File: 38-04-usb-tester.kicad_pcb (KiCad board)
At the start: 2 copper layers, 101.7 x 101.7 mm, 33 parts, among them J1 USB3_A, J2 USB_B_Micro, J3 USB_C_Receptacle, J4 USB_B_Mini

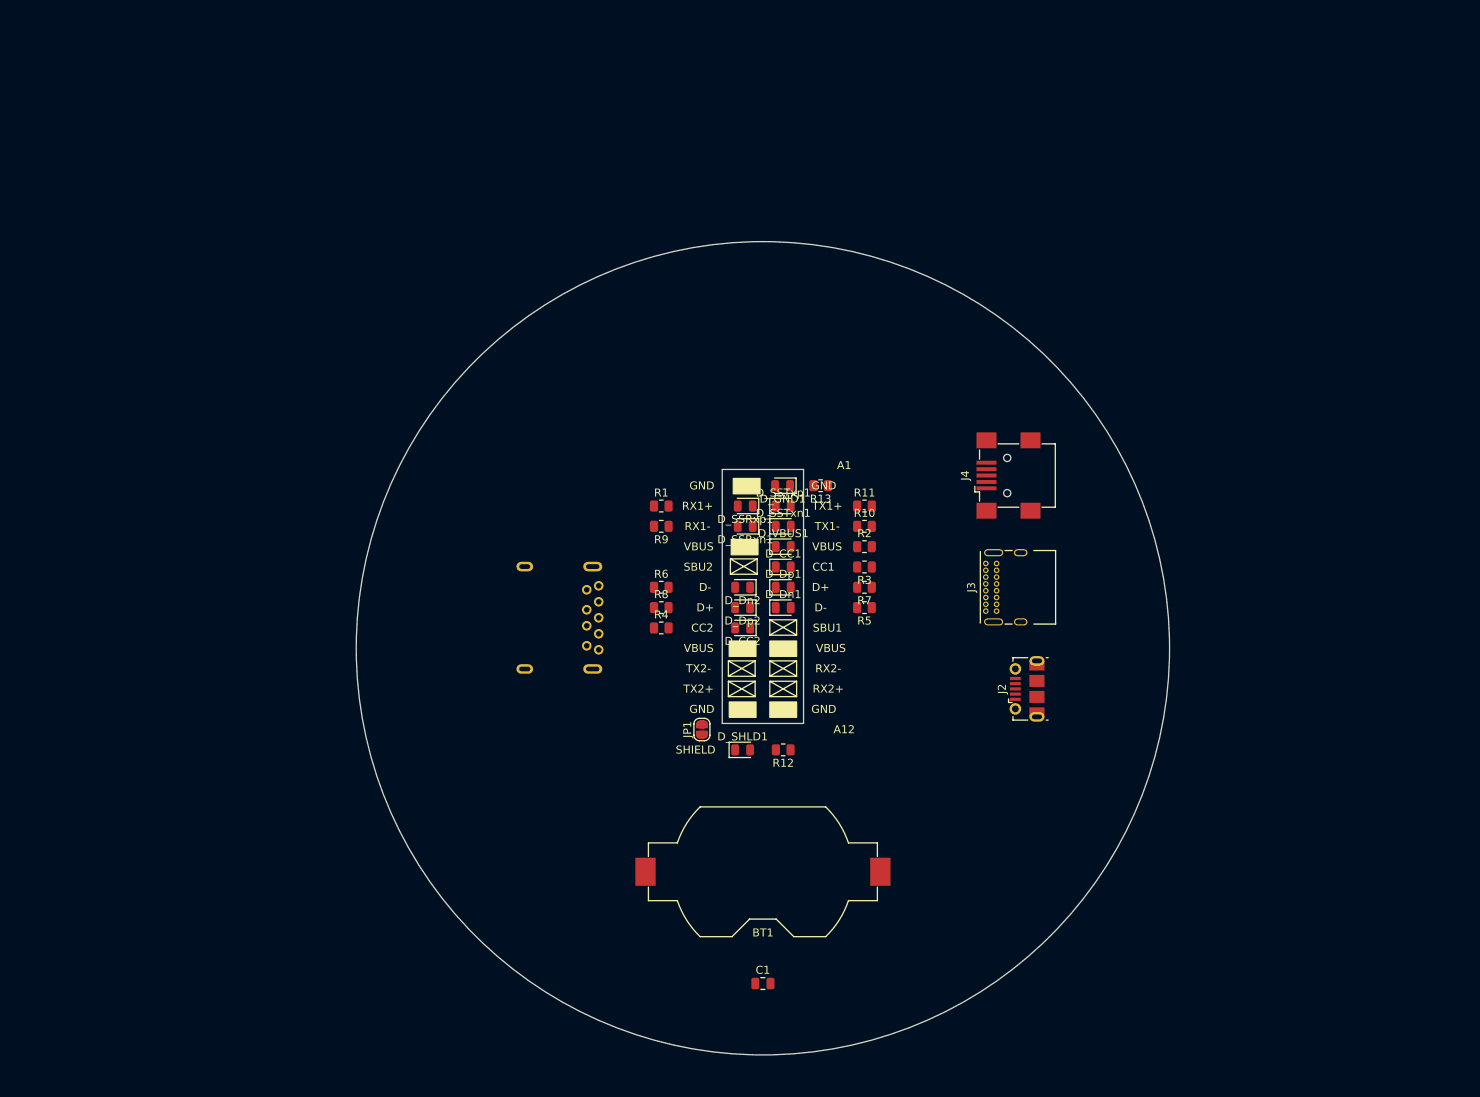
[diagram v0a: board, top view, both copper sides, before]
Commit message: added new footprints, schematic edits
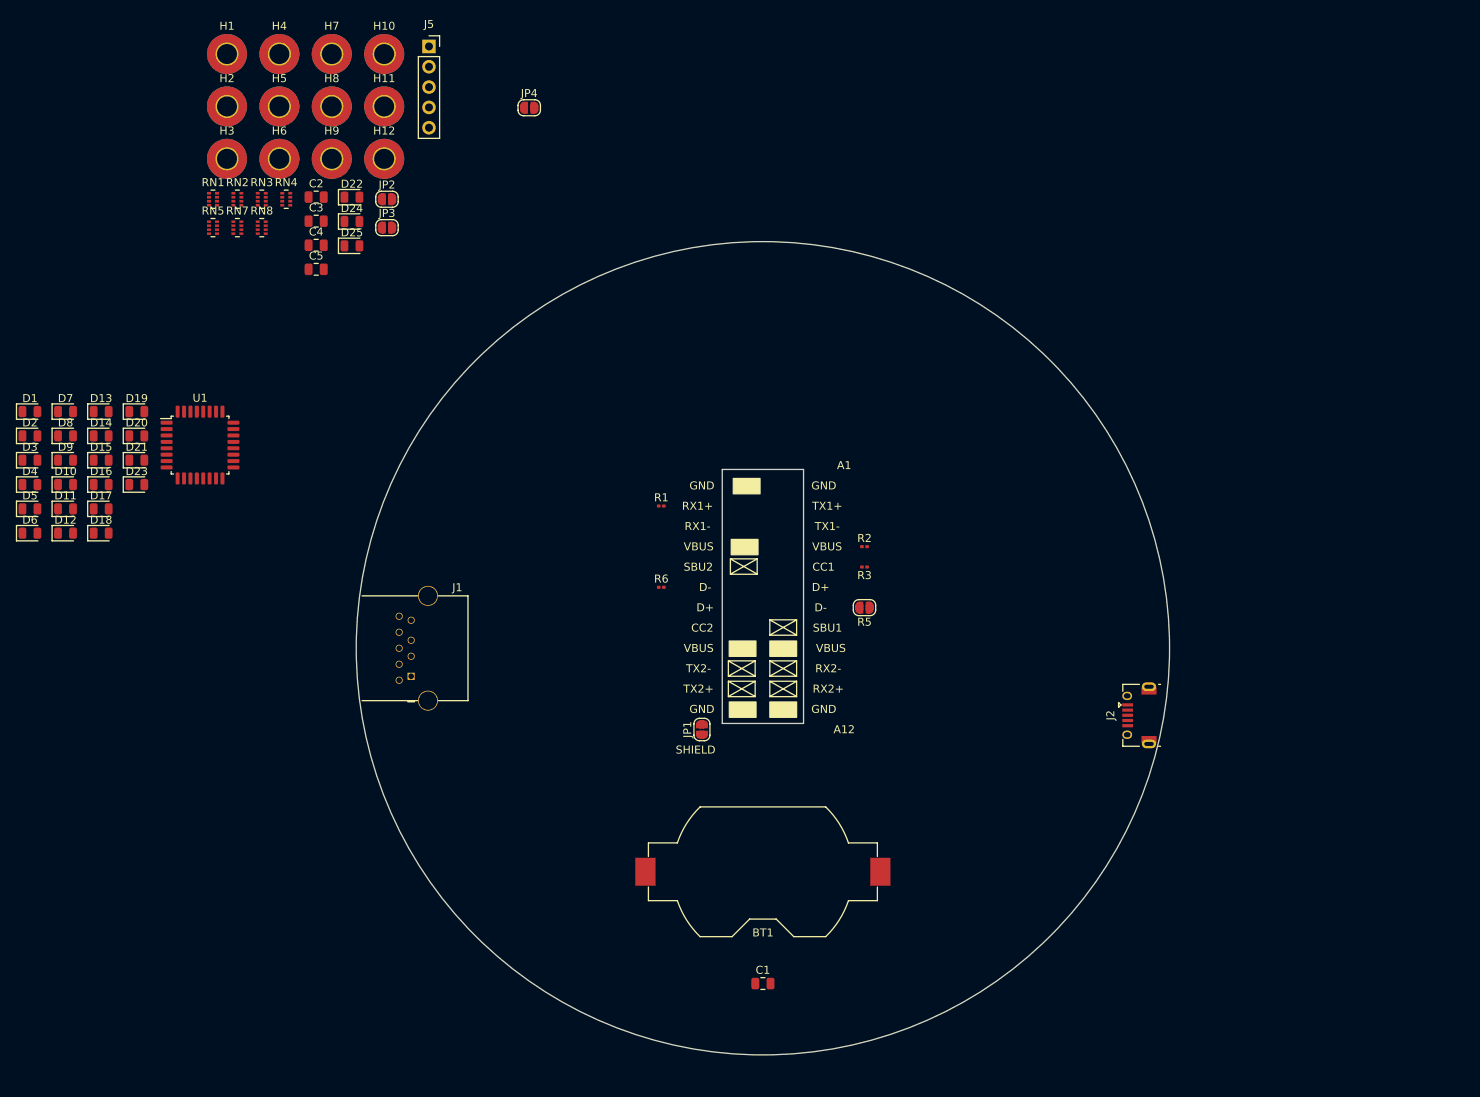
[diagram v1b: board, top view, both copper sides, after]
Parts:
- removed D_CC1, D_CC2, D_Dn1, D_Dn2, D_Dp1, D_Dp2, D_GND1, D_SHLD1, D_SSRxn1, D_SSRxp1, D_SSTxn1, D_SSTxp1, D_VBUS1: LED, LED_SMD:LED_0805_2012Metric
- removed J3: USB_C_Receptacle, Connector_USB:USB_C_Receptacle_GCT_USB4085
- removed J4: USB_B_Mini, Connector_USB:USB_Mini-B_Wuerth_65100516121_Horizontal
- removed R10, R11, R12, R13, R4, R7, R8, R9: 100, Resistor_SMD:R_0805_2012Metric
- added C2: 100n, Capacitor_SMD:C_0805_2012Metric, F.Cu at (99.1, 54.1)
- added C3: 100n, Capacitor_SMD:C_0805_2012Metric, F.Cu at (99.1, 57.1)
- added C4: 100n, Capacitor_SMD:C_0805_2012Metric, F.Cu at (99.1, 60.1)
- added C5: 4u7, Capacitor_SMD:C_0805_2012Metric, F.Cu at (99.1, 63.1)
- added D1: SSRx2+_D, LED_SMD:LED_0805_2012Metric, F.Cu at (63.3, 80.9)
- added D10: SSRx1+_D, LED_SMD:LED_0805_2012Metric, F.Cu at (67.8, 90.0)
- added D11: SSRx1-_D, LED_SMD:LED_0805_2012Metric, F.Cu at (67.8, 93.1)
- added D12: SSRx2-_D, LED_SMD:LED_0805_2012Metric, F.Cu at (67.8, 96.1)
- added D13: SSRx2+_D, LED_SMD:LED_0805_2012Metric, F.Cu at (72.2, 80.9)
- added D14: GND_D, LED_SMD:LED_0805_2012Metric, F.Cu at (72.2, 83.9)
- added D15: VBUS_LED_D, LED_SMD:LED_0805_2012Metric, F.Cu at (72.2, 87.0)
- added D16: CC_NORM_D, LED_SMD:LED_0805_2012Metric, F.Cu at (72.2, 90.0)
- added D17: CC_REV_D, LED_SMD:LED_0805_2012Metric, F.Cu at (72.2, 93.1)
- added D18: Rp_D, LED_SMD:LED_0805_2012Metric, F.Cu at (72.2, 96.1)
- added D19: Rd_D, LED_SMD:LED_0805_2012Metric, F.Cu at (76.7, 80.9)
- added D2: SSRx1+_D, LED_SMD:LED_0805_2012Metric, F.Cu at (63.3, 83.9)
- added D20: Ra_D, LED_SMD:LED_0805_2012Metric, F.Cu at (76.7, 83.9)
- added D21: OTG_D, LED_SMD:LED_0805_2012Metric, F.Cu at (76.7, 87.0)
- added D22: Power, LED_SMD:LED_0805_2012Metric, F.Cu at (103.6, 54.1)
- added D23: SSRx2-_D, LED_SMD:LED_0805_2012Metric, F.Cu at (76.7, 90.0)
- added D24: CC_bb_D, LED_SMD:LED_0805_2012Metric, F.Cu at (103.6, 57.1)
- added D25: CC_ba_D, LED_SMD:LED_0805_2012Metric, F.Cu at (103.6, 60.2)
- added D3: SSRx1-_D, LED_SMD:LED_0805_2012Metric, F.Cu at (63.3, 87.0)
- added D4: SSTx2-_D, LED_SMD:LED_0805_2012Metric, F.Cu at (63.3, 90.0)
- added D5: SSTx2+_D, LED_SMD:LED_0805_2012Metric, F.Cu at (63.3, 93.1)
- added D6: SSTx1+_D, LED_SMD:LED_0805_2012Metric, F.Cu at (63.3, 96.1)
- added D7: SSTx1-_D, LED_SMD:LED_0805_2012Metric, F.Cu at (67.8, 80.9)
- added D8: SSRx2-_D, LED_SMD:LED_0805_2012Metric, F.Cu at (67.8, 83.9)
- added D9: SSRx2+_D, LED_SMD:LED_0805_2012Metric, F.Cu at (67.8, 87.0)
- added H1: B_CC1, MountingHole:MountingHole_2.5mm_Pad_TopBottom, F.Cu at (88.0, 36.2)
- added H10: A_GND, MountingHole:MountingHole_2.5mm_Pad_TopBottom, F.Cu at (107.6, 36.2)
- added H11: B_VBUS, MountingHole:MountingHole_2.5mm_Pad_TopBottom, F.Cu at (107.6, 42.8)
- added H12: B_GND, MountingHole:MountingHole_2.5mm_Pad_TopBottom, F.Cu at (107.6, 49.3)
- added H2: B_CC2, MountingHole:MountingHole_2.5mm_Pad_TopBottom, F.Cu at (88.0, 42.8)
- added H3: A_CC2, MountingHole:MountingHole_2.5mm_Pad_TopBottom, F.Cu at (88.0, 49.3)
- added H4: A_CC1, MountingHole:MountingHole_2.5mm_Pad_TopBottom, F.Cu at (94.5, 36.2)
- added H5: ID, MountingHole:MountingHole_2.5mm_Pad_TopBottom, F.Cu at (94.5, 42.8)
- added H6: B_SHIELD, MountingHole:MountingHole_2.5mm_Pad_TopBottom, F.Cu at (94.5, 49.3)
- added H7: A_SHIELD, MountingHole:MountingHole_2.5mm_Pad_TopBottom, F.Cu at (101.0, 36.2)
- added H8: A_DRAIN, MountingHole:MountingHole_2.5mm_Pad_TopBottom, F.Cu at (101.0, 42.8)
- added H9: A_VBUS, MountingHole:MountingHole_2.5mm_Pad_TopBottom, F.Cu at (101.0, 49.3)
- added J5: Conn_01x05_Pin, Connector_PinSocket_2.54mm:PinSocket_1x05_P2.54mm_Vertical, F.Cu at (113.2, 35.3)
- added JP2: SolderJumper_2_Bridged, Jumper:SolderJumper-2_P1.3mm_Open_RoundedPad1.0x1.5mm, F.Cu at (108.0, 54.4)
- added JP3: SolderJumper_2_Bridged, Jumper:SolderJumper-2_P1.3mm_Open_RoundedPad1.0x1.5mm, F.Cu at (108.0, 57.9)
- added JP4: SolderJumper_2_Bridged, Jumper:SolderJumper-2_P1.3mm_Open_RoundedPad1.0x1.5mm, F.Cu at (125.7, 42.9)
- added RN1: 10K, Resistor_SMD:R_Array_Concave_4x0402, F.Cu at (86.2, 54.4)
- added RN2: 10K, Resistor_SMD:R_Array_Concave_4x0402, F.Cu at (89.2, 54.4)
- added RN3: 10K, Resistor_SMD:R_Array_Concave_4x0402, F.Cu at (92.3, 54.4)
- added RN4: 10K, Resistor_SMD:R_Array_Concave_4x0402, F.Cu at (95.3, 54.4)
- added RN5: 10K, Resistor_SMD:R_Array_Concave_4x0402, F.Cu at (86.2, 57.9)
- added RN7: 10K, Resistor_SMD:R_Array_Concave_4x0402, F.Cu at (89.2, 57.9)
- added RN8: 10K, Resistor_SMD:R_Array_Concave_4x0402, F.Cu at (92.3, 57.9)
- added U1: STM32C031K6Tx, Package_QFP:LQFP-32_7x7mm_P0.8mm, F.Cu at (84.6, 85.1)
- J1: value USB3_A -> HC-USB3.0-L168-WP; footprint Connector_USB:USB3_A_Molex_48393-001 -> 01-UserLibary:HC-USB3.0-L168-WP_USB-A_THT-9-2MP_P2.0mm; moved to F.Cu
- J2: value USB_B_Micro -> USB-B-Micro; footprint Connector_USB:USB_Micro-B_Molex-105017-0001 -> 01-UserLibary:USB_Micro-B_Kinghelm-KH-MICRO5P-JN
- JP1: value SolderJumper_2_Open -> SolderJumper_2_Bridged
- R1, R2, R3, R6: value 100 -> 10k; footprint Resistor_SMD:R_0805_2012Metric -> Resistor_SMD:R_0201_0603Metric
- R5: value 100 -> 2k; footprint Resistor_SMD:R_0805_2012Metric -> Jumper:SolderJumper-2_P1.3mm_Open_RoundedPad1.0x1.5mm
- moved J1 23.4 mm to (109.5, 110.5)
- moved J2 15.6 mm to (203.2, 118.9)
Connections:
- BT1 pad 1: /Vcc -> Net-(BT1-+)
- C1 pad 1: /Vcc -> Net-(BT1-+)
- J1 pad 1: /Vcc -> /A_VBUS
- J1 pad 2: /Vcc -> /A_D1-_D
- J1 pad 3: /Vcc -> /A_D1+_D
- J1 pad 4: /Vcc -> /A_GND
- J1 pad 5: /Vcc -> /A_SSRx1-
- J1 pad 6: /Vcc -> /A_SSRx1+
- J1 pad 7: /Vcc -> /A_DRAIN
- J1 pad 8: /Vcc -> /A_SSTx1-
- J1 pad 9: /Vcc -> /A_SSTx1+
- J2 pad 1: /VBUS -> /B_VBUS_A4
- J2 pad 2: /Dn1 -> /B_D1-
- J2 pad 3: /Dp1 -> /B_D1+
- J2 pad 4: unconnected-(J2-Pad4) -> /ID
- J2 pad 5: /GROUND -> GND
- J2 pad 6: /SHIELD -> /B_SHIELD
- JP1 pad 1: /SHIELD -> /A_GND
- JP1 pad 2: /GROUND -> /A_GND_SENS
- R1 pad 1: unconnected-(R1-Pad1) -> /CC2_CTRL
- R1 pad 2: Net-(D_SSRxp1-Pad2) -> /B_CC2_SENS
- R2 pad 1: /VBUS -> /CC1_CTRL
- R2 pad 2: Net-(D_VBUS1-Pad2) -> /B_CC1_SENS
- R3 pad 1: /CC1 -> VCC
- R5 pad 1: /Dn1 -> VCC
- R6 pad 1: /Dn2 -> /A_VBUS_SENS
- R6 pad 2: Net-(D_Dn2-Pad2) -> GND

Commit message: mini b and dip switch footprint and schems
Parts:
- removed JP1, JP2, JP3, JP4: SolderJumper_2_Bridged, Jumper:SolderJumper-2_P1.3mm_Open_RoundedPad1.0x1.5mm
- added J3: USB_C_12401832E402A, 01-UserLibary:USB_C_Receptacle_Amphenol_12401832E402A, F.Cu at (198.4, 94.5)
- added J4: USB_Mini-B_U-M-M5DD-W-1, 01-UserLibary:USB_Mini-B_Korean-Hroparts_U-M-M5DD-W-1_SMD-5-4MP, F.Cu at (197.9, 106.4)
- added J6: USB_C_12401832E402A, 01-UserLibary:USB_C_Receptacle_Amphenol_12401832E402A, F.Cu at (111.0, 94.2)
- added SW3: ~, 01-UserLibary:SW-DIP-4P_P1.27mm_SMD-2x4, F.Cu at (181.1, 125.0)
- J1: footprint 01-UserLibary:HC-USB3.0-L168-WP_USB-A_THT-9-2MP_P2.0mm -> 01-UserLibary:USB_A_Hong-Cheng_HC-USB3.0-L168-WP_THT-9-2MP_P2.0mm
- J2: value USB-B-Micro -> USB_Micro-B_KH-MICRO5P-JN
